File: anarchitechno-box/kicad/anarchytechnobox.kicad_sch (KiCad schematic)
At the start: 27 parts, among them J3 Screw_Terminal_01x03, J4 Screw_Terminal_01x03, J5 Screw_Terminal_01x03, J6 Screw_Terminal_01x03

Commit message: derp
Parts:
- gave numbers to parts that had none: 1
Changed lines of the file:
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@@
 		(dnp no)
 		(fields_autoplaced yes)
-		(property "Reference" "M?"
+		(property "Reference" "M1"
 			(at 271.78 190.4999 0)
 			(effects
@@
 			(project "anarchytechnobox"
 				(path "/8c734c41-38ed-40fc-83bd-134786dcfb35"
-					(reference "M?")
+					(reference "M1")
 					(unit 1)
 				)

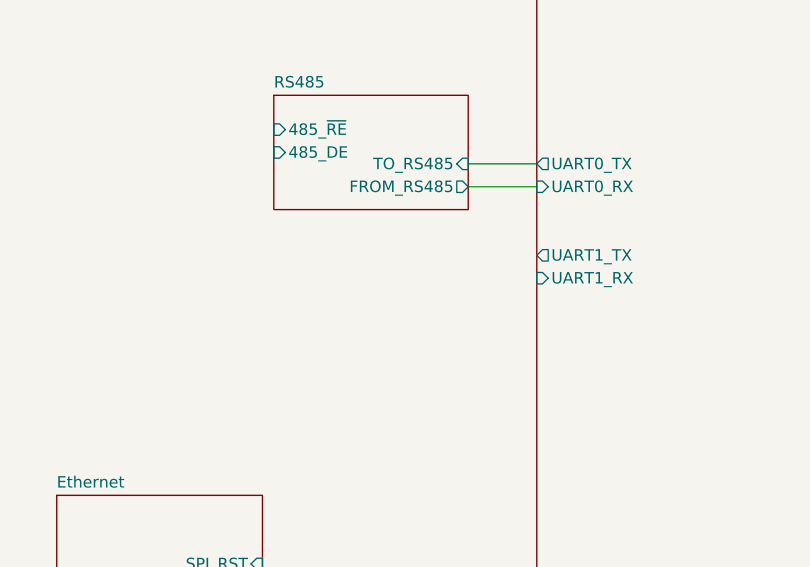
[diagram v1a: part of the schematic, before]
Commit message: MIDI input using autosensing TRS midi jack
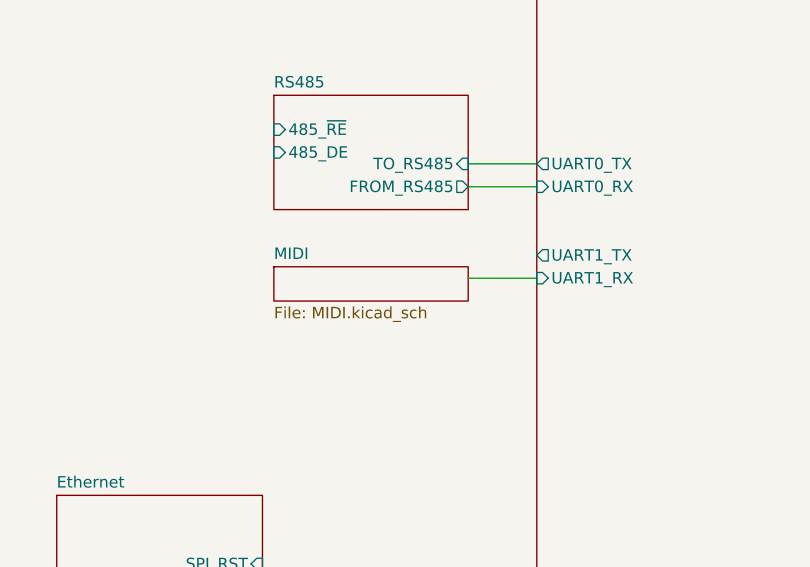
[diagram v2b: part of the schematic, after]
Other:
- added sheet MIDI (MIDI.kicad_sch)
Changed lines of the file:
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@@
 	(wire
 		(pts
+			(xy 99.06 99.06) (xy 91.44 99.06)
+		)
+		(stroke
+			(width 0)
+			(type default)
+		)
+	)
+	(wire
+		(pts
 			(xy 146.05 39.37) (xy 309.88 39.37)
 		)
@@
 				)
 			)
+		)
+	)
+	(sheet
+		(at 69.85 97.79)
+		(size 21.59 3.81)
+		(exclude_from_sim no)
+		(in_bom yes)
+		(on_board yes)
+		(dnp no)
+		(fields_autoplaced yes)
+		(stroke
+			(width 0.1524)
+			(type solid)
+		)
+		(fill
+			(color 0 0 0 0.0000)
+		)
+		(property "Sheetname" "MIDI"
+			(at 69.85 97.0784 0)
+			(effects
+				(font
+					(size 1.27 1.27)
+				)
+				(justify left bottom)
+			)
+		)
+		(property "Sheetfile" "MIDI.kicad_sch"
+			(at 69.85 102.1846 0)
+			(effects
+				(font
+					(size 1.27 1.27)
+				)
+				(justify left top)
+			)
+		)
+		(instances
+			(project "anarchytechnobox"
+				(path "/8c734c41-38ed-40fc-83bd-134786dcfb35"
+					(page "13")
+				)
+			)

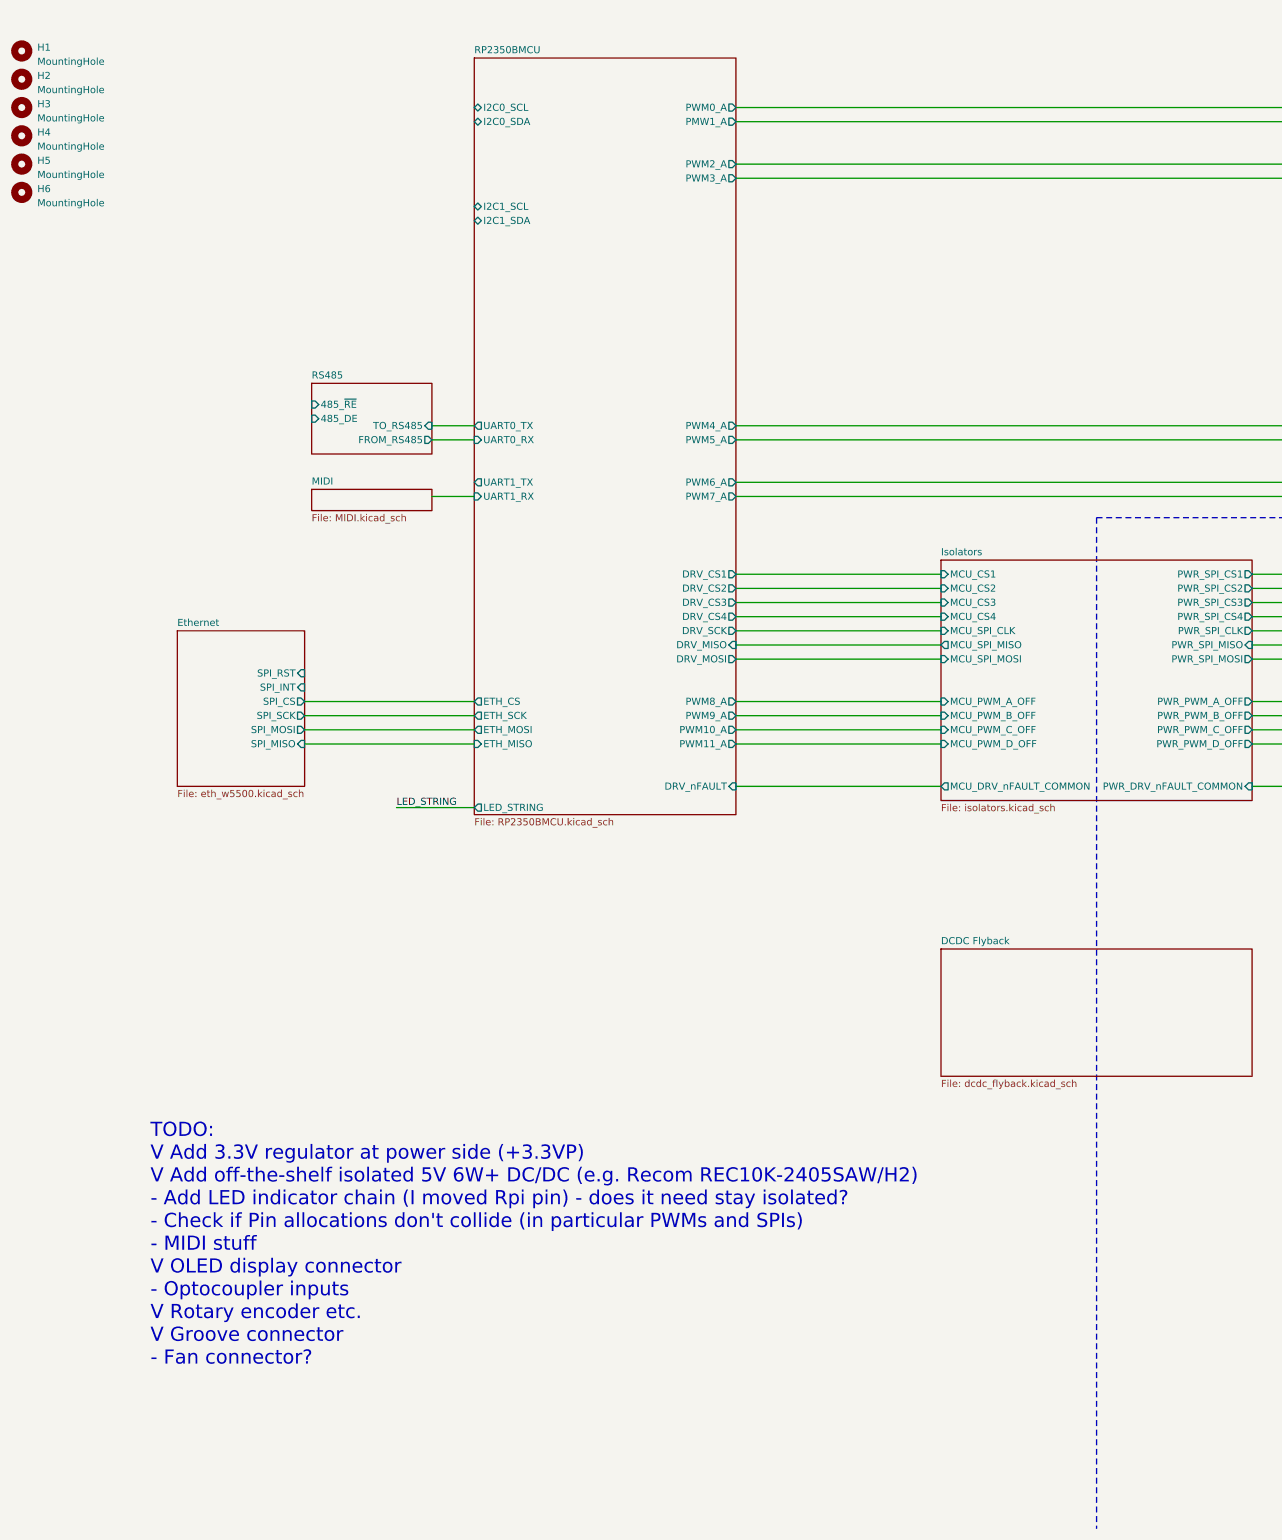
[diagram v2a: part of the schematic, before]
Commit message: Schematic & PCB changes: - Cleaned up unnecessary electrolytic input capacitor flyback - Removed dual diode rectification on 5V, increased output capacitors - Feedback resistors DC/DCs set, enlarged for JLC basic parts - Sweep through schematic to consolidate caps to JLC basic parts (see list schematic front page) - Midi OUTPUT added (please check schematic) - Wiznet W5500 schematic reworked to RJ45 reference schematic: https://docs.wiznet.io/assets/files/w5500_sch_v110_use_mag_-dfff8bbb103d13be4f25cd2b2f8b950d.pdf - Replaced ethernet jack to HR911105A - Crystals chosen for W5500 and RP2350B (according to reference), 15pF load caps. - RS485 driver changed to SP3485EN for 3.3V operation - Replaced RS485 bus connectors with 2x RJ45s for passthrough - Groove connector replaced with JST XH 2mm - Added LCSC part numbers for various components in the schematic
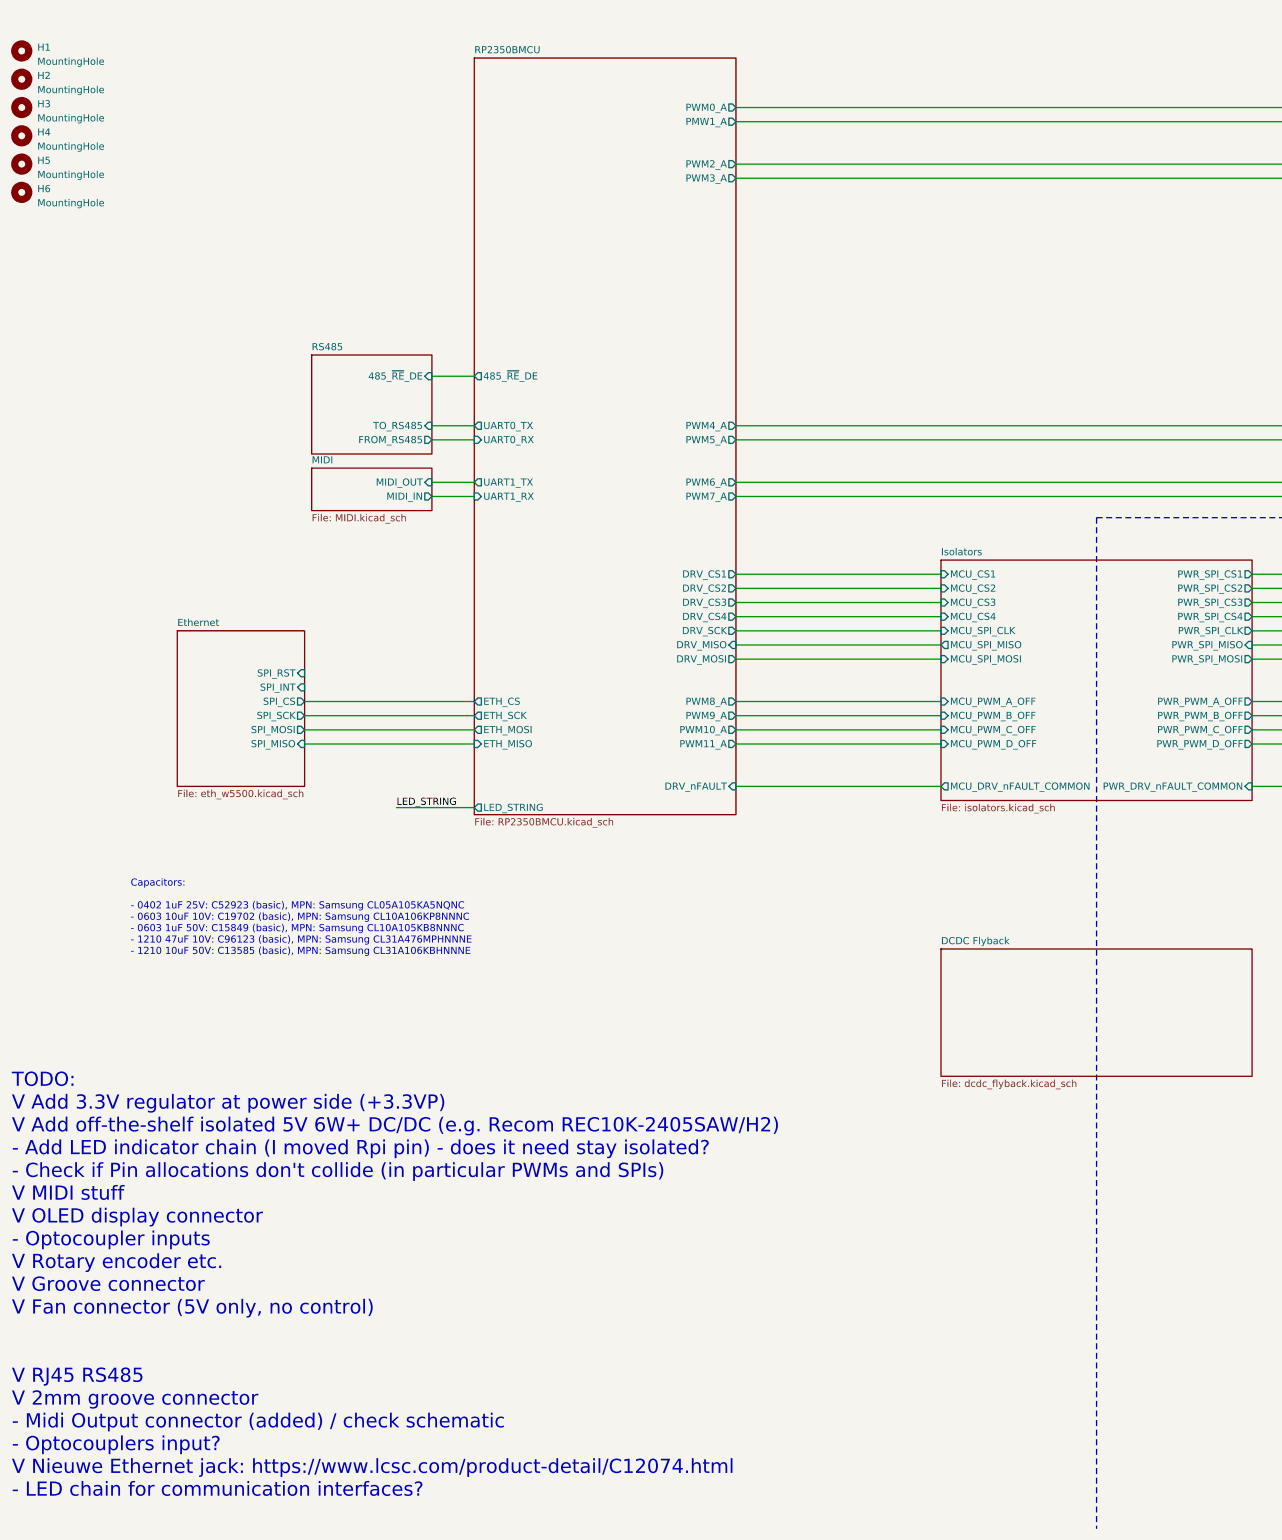
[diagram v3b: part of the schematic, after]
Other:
- sheet MIDI ports: added MIDI_IN, MIDI_OUT; removed none
- sheet RP2350BMCU ports: added 485_~{RE}_DE; removed I2C0_SCL, I2C0_SDA, I2C1_SCL, I2C1_SDA
- sheet RS485 ports: added 485_~{RE}_DE; removed 485_DE, 485_~{RE}
- note added: "Capacitors: - 0402 1uF 25V: C52923 (basic), MPN: Samsung CL05A105KA5NQNC - 0603 10uF 10V: C19702 (basic), MPN: Samsung CL10A106KP8NNNC - 0603 1uF 50V: C15849 (basic), MPN: Samsung CL10A105KB8NNNC - 1210 47uF 10V: C96123 (basic), MPN: Samsung CL31A476MPHNNNE - 1210 10uF 50V: C13585 (basic), MPN: Samsung CL31A106KBHNNNE"
- note added: "TODO: V Add 3.3V regulator at power side (+3.3VP) V Add off-the-shelf isolated 5V 6W+ DC/DC (e.g. Recom REC10K-2405SAW/H2) - Add LED indicator chain (I moved Rpi pin) - does it need stay isolated? - Check if Pin allocations don't collide (in particular PWMs and SPIs) V MIDI stuff V OLED display connector - Optocoupler inputs V Rotary encoder etc. V Groove connector V Fan connector (5V only, no co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"
- note removed: "TODO: V Add 3.3V regulator at power side (+3.3VP) V Add off-the-shelf isolated 5V 6W+ DC/DC (e.g. Recom REC10K-2405SAW/H2) - Add LED indicator chain (I moved Rpi pin) - does it need stay isolated? - Check if Pin allocations don't collide (in particular PWMs and SPIs) - MIDI stuff V OLED display connector - Optocoupler inputs V Rotary encoder etc. V Groove connector - Fan connector?"
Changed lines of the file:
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@@
 		)
 	)
-	(text "TODO:\nV Add 3.3V regulator at power side (+3.3VP)\nV Add off-the-shelf isolated 5V 6W+ DC/DC (e.g. Recom REC10K-2405SAW/H2)\n- Add LED indicator chain (I moved Rpi pin) - does it need stay isolated?\n- Check if Pin allocations don't collide (in particular PWMs and SPIs)\n- MIDI stuff\nV OLED display connector\n- Optocoupler inputs\nV Rotary encoder etc.\nV Groove connector\n- Fan connector?"
+	(text "Capacitors:\n\n- 0402 1uF 25V: C52923 (basic), MPN: Samsung CL05A105KA5NQNC\n- 0603 10uF 10V: C19702 (basic), MPN: Samsung CL10A106KP8NNNC\n- 0603 1uF 50V: C15849 (basic), MPN: Samsung CL10A105KB8NNNC\n- 1210 47uF 10V: C96123 (basic), MPN: Samsung CL31A476MPHNNNE\n- 1210 10uF 50V: C13585 (basic), MPN: Samsung CL31A106KBHNNNE"
 		(exclude_from_sim no)
-		(at 40.894 233.426 0)
+		(at 37.338 174.752 0)
+		(effects
+			(font
+				(size 1.27 1.27)
+			)
+			(justify left)
+		)
+	)
+	(text "TODO:\nV Add 3.3V regulator at power side (+3.3VP)\nV Add off-the-shelf isolated 5V 6W+ DC/DC (e.g. Recom REC10K-2405SAW/H2)\n- Add LED indicator chain (I moved Rpi pin) - does it need stay isolated?\n- Check if Pin allocations don't collide (in particular PWMs and SPIs)\nV MIDI stuff\nV OLED display connector\n- Optocoupler inputs\nV Rotary encoder etc.\nV Groove connector\nV Fan connector (5V only, no control)\n\n\nV RJ45 RS485\nV 2mm groove connector\n- Midi Output connector (added) / check schematic\n- Optocouplers input?\nV Nieuwe Ethernet jack: https://www.lcsc.com/product-detail/C12074.html\n- LED chain for communication interfaces?"
+		(exclude_from_sim no)
+		(at 16.002 240.792 0)
 		(effects
 			(font
@@
 	(wire
 		(pts
+			(xy 91.44 77.47) (xy 99.06 77.47)
+		)
+		(stroke
+			(width 0)
+			(type default)
+		)
+	)
+	(wire
+		(pts
+			(xy 91.44 96.52) (xy 99.06 96.52)
+		)
+		(stroke
+			(width 0)
+			(type default)
+		)
+	)
+	(wire
+		(pts
 			(xy 68.58 138.43) (xy 99.06 138.43)
 		)
@@
 	)
 	(sheet
-		(at 69.85 78.74)
-		(size 21.59 12.7)
+		(at 69.85 73.66)
+		(size 21.59 17.78)
 		(exclude_from_sim no)
 		(in_bom yes)
@@
 		)
 		(property "Sheetname" "RS485"
-			(at 69.85 78.0284 0)
+			(at 69.85 72.9484 0)
 			(effects
 				(font
@@
 			)
 		)
-		(pin "485_~{RE}" input
-			(at 69.85 82.55 180)
-			(effects
-				(font
-					(size 1.27 1.27)
-				)
-				(justify left)
-			)
-		)
 		(pin "FROM_RS485" output
 			(at 91.44 88.9 0)
@@
 			)
 		)
-		(pin "485_DE" input
-			(at 69.85 85.09 180)
+		(pin "TO_RS485" input
+			(at 91.44 86.36 0)
 			(effects
 				(font
 					(size 1.27 1.27)
 				)
-				(justify left)
+				(justify right)
 			)
 		)
-		(pin "TO_RS485" input
-			(at 91.44 86.36 0)
+		(pin "485_~{RE}_DE" input
+			(at 91.44 77.47 0)
 			(effects
 				(font
@@
 			)
 		)
-		(pin "I2C0_SCL" bidirectional
-			(at 99.06 29.21 180)
-			(effects
-				(font
-					(size 1.27 1.27)
-				)
-				(justify left)
-			)
-		)
-		(pin "I2C0_SDA" bidirectional
-			(at 99.06 31.75 180)
-			(effects
-				(font
-					(size 1.27 1.27)
-				)
-				(justify left)
-			)
-		)
-		(pin "I2C1_SDA" bidirectional
-			(at 99.06 49.53 180)
-			(effects
-				(font
-					(size 1.27 1.27)
-				)
-				(justify left)
-			)
-		)
-		(pin "I2C1_SCL" bidirectional
-			(at 99.06 46.99 180)
-			(effects
-				(font
-					(size 1.27 1.27)
-				)
-				(justify left)
-			)
-		)
 		(pin "UART1_TX" output
 			(at 99.06 96.52 180)
@@
 			)
 		)
+		(pin "485_~{RE}_DE" output
+			(at 99.06 77.47 180)
+			(effects
+				(font
+					(size 1.27 1.27)
+				)
+				(justify left)
+			)
+		)
 		(instances
 			(project "anarchytechnobox"
@@
 	)
 	(sheet
-		(at 69.85 97.79)
-		(size 21.59 3.81)
+		(at 69.85 93.98)
+		(size 21.59 7.62)
 		(exclude_from_sim no)
 		(in_bom yes)
@@
 		)
 		(property "Sheetname" "MIDI"
-			(at 69.85 97.0784 0)
+			(at 69.85 93.2684 0)
 			(effects
 				(font
@@
 			)
 		)
+		(pin "MIDI_IN" output
+			(at 91.44 99.06 0)
+			(effects
+				(font
+					(size 1.27 1.27)
+				)
+				(justify right)
+			)
+		)
+		(pin "MIDI_OUT" input
+			(at 91.44 96.52 0)
+			(effects
+				(font
+					(size 1.27 1.27)
+				)
+				(justify right)
+			)
+		)

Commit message: - Thermische berekening DRV8245 vs losse transistors - DRV8245 package gecorrigeerd naar TSSOP-28 - Layout aangepast om grotere package te passen - 1x GND output per kanaal - Waarschijnlijk geen 140mm fan nodig => print weer gekropmen - RS485 power line gefixed (3.3V vs 3V3P) - Kleine BOM en I/O wijzigingen tbv layout
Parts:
- H2, H5: now not fitted; now left out of the parts list
- J3, J4, J5, J6: footprint TerminalBlock_Phoenix:TerminalBlock_Phoenix_MKDS-1,5-3-5.08_1x03_P5.08mm_Horizontal -> TerminalBlock_Phoenix:TerminalBlock_Phoenix_MKDS-1,5-4-5.08_1x04_P5.08mm_Horizontal; symbol Connector:Screw_Terminal_01x03 -> Connector:Screw_Terminal_01x04
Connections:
- net GND2: now also J3.3 (Pin_3), J4.3 (Pin_3), J5.3 (Pin_3), J6.3 (Pin_3)
- net HB_1_OUT_B: now also J3.4 (Pin_4); no longer J3.3 (Pin_3)
- net HB_1_OUT_D: now also J4.4 (Pin_4); no longer J4.3 (Pin_3)
- net HB_2_OUT_B: now also J5.4 (Pin_4); no longer J5.3 (Pin_3)
- net HB_2_OUT_D: now also J6.4 (Pin_4); no longer J6.3 (Pin_3)
